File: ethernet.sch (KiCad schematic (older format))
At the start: 57 parts, among them J1701 RJ45, U1701 AR8031, Y1701 25MHz

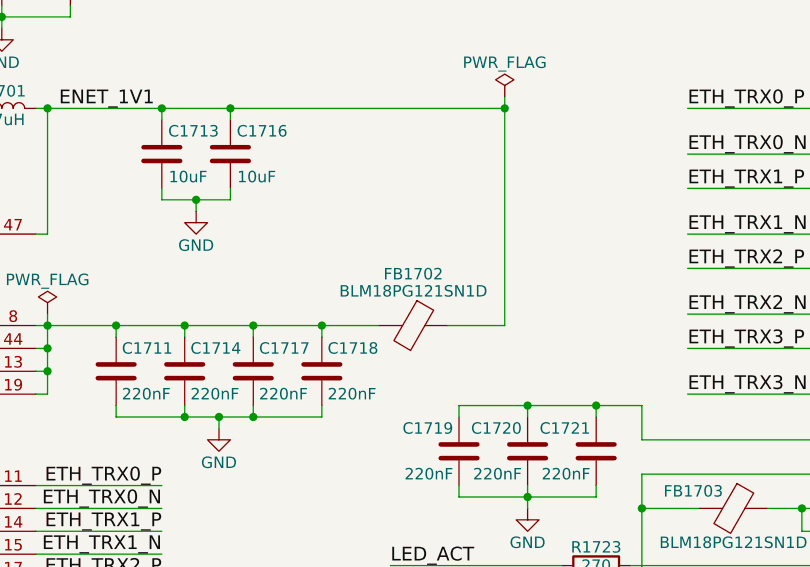
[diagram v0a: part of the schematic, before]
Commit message: Now using GPIO5_IO03 (P4.03) to put the class-D op-amp in shutdown and conserve energy when muted, make C1716 near the ETH PHY's DVDDL pin 47 220nF instead of 10uF (EmCraft suggested that this should be 100nF but their's is 220nF, asked why), added a 10k pull-down to PAM2841's ENA pin, added a 100nF cap to the smart card's C1 VCC pin, added a 1uF cap to the haptic motor circuit's 3V3_P rail
Still need to use I2C3 instead of I2C1 according to EmCraft's suggestions.
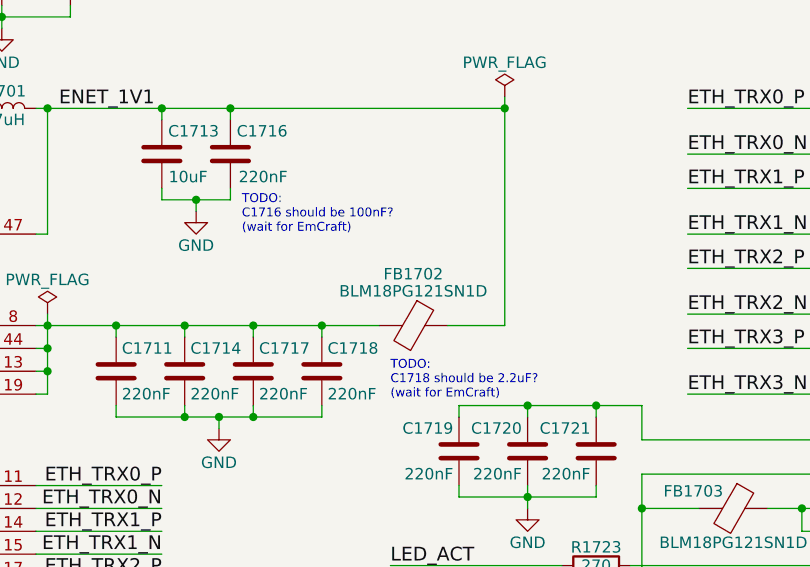
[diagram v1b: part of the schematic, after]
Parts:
- C1716: value 10uF -> 220nF
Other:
- note added: "TODO:\nC1716 should be 100nF?\n(wait for EmCraft)"
- note added: "TODO:\nC1718 should be 2.2uF?\n(wait for EmCraft)"
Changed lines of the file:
@@
 $EndComp
 $Comp
-L GND #PWR0296
+L GND #PWR0297
 U 1 1 5AF1A655
 P 5100 6650
-F 0 "#PWR0296" H 5100 6400 50  0001 C CNN
+F 0 "#PWR0297" H 5100 6400 50  0001 C CNN
 F 1 "GND" H 5100 6500 50  0000 C CNN
 F 2 "" H 5100 6650 50  0001 C CNN
@@
 $EndComp
 $Comp
-L GND #PWR0297
+L GND #PWR0298
 U 1 1 5AF1A6B7
 P 4000 6700
-F 0 "#PWR0297" H 4000 6450 50  0001 C CNN
+F 0 "#PWR0298" H 4000 6450 50  0001 C CNN
 F 1 "GND" H 4000 6550 50  0000 C CNN
 F 2 "" H 4000 6700 50  0001 C CNN
@@
 $EndComp
 $Comp
-L GND #PWR0298
+L GND #PWR0299
 U 1 1 5AF1C035
 P 3050 6900
-F 0 "#PWR0298" H 3050 6650 50  0001 C CNN
+F 0 "#PWR0299" H 3050 6650 50  0001 C CNN
 F 1 "GND" H 3050 6750 50  0000 C CNN
 F 2 "" H 3050 6900 50  0001 C CNN
@@
 $EndComp
 $Comp
-L GND #PWR0299
+L GND #PWR0300
 U 1 1 5AF1D077
 P 2150 6550
-F 0 "#PWR0299" H 2150 6300 50  0001 C CNN
+F 0 "#PWR0300" H 2150 6300 50  0001 C CNN
 F 1 "GND" H 2150 6400 50  0000 C CNN
 F 2 "" H 2150 6550 50  0001 C CNN
@@
 $EndComp
 $Comp
-L GND #PWR0300
+L GND #PWR0301
 U 1 1 5AF23D63
 P 6500 6550
-F 0 "#PWR0300" H 6500 6300 50  0001 C CNN
+F 0 "#PWR0301" H 6500 6300 50  0001 C CNN
 F 1 "GND" H 6500 6400 50  0000 C CNN
 F 2 "" H 6500 6550 50  0001 C CNN
@@
 $EndComp
 $Comp
-L GND #PWR0301
+L GND #PWR0302
 U 1 1 5AF27185
 P 6950 3550
-F 0 "#PWR0301" H 6950 3300 50  0001 C CNN
+F 0 "#PWR0302" H 6950 3300 50  0001 C CNN
 F 1 "GND" H 6950 3400 50  0000 C CNN
 F 2 "" H 6950 3550 50  0001 C CNN
@@
 $EndComp
 $Comp
-L GND #PWR0302
+L GND #PWR0303
 U 1 1 5AF2ADD1
 P 6850 2600
-F 0 "#PWR0302" H 6850 2350 50  0001 C CNN
+F 0 "#PWR0303" H 6850 2350 50  0001 C CNN
 F 1 "GND" H 6850 2450 50  0000 C CNN
 F 2 "" H 6850 2600 50  0001 C CNN
@@
 $EndComp
 $Comp
-L GND #PWR0303
+L GND #PWR0304
 U 1 1 5AF2DC02
 P 4200 1450
-F 0 "#PWR0303" H 4200 1200 50  0001 C CNN
+F 0 "#PWR0304" H 4200 1200 50  0001 C CNN
 F 1 "GND" H 4200 1300 50  0000 C CNN
 F 2 "" H 4200 1450 50  0001 C CNN
@@
 $EndComp
 $Comp
-L GND #PWR0304
+L GND #PWR0305
 U 1 1 5AF2E0B5
 P 4200 2100
-F 0 "#PWR0304" H 4200 1850 50  0001 C CNN
+F 0 "#PWR0305" H 4200 1850 50  0001 C CNN
 F 1 "GND" H 4200 1950 50  0000 C CNN
 F 2 "" H 4200 2100 50  0001 C CNN
@@
 $EndComp
 $Comp
-L 3V3_P #PWR0305
+L 3V3_P #PWR0306
 U 1 1 5AF325F5
 P 3000 950
-F 0 "#PWR0305" H 3000 800 50  0001 C CNN
+F 0 "#PWR0306" H 3000 800 50  0001 C CNN
 F 1 "3V3_P" H 3000 1090 50  0000 C CNN
 F 2 "" H 3000 950 50  0001 C CNN
@@
 $EndComp
 $Comp
-L GND #PWR0306
+L GND #PWR0307
 U 1 1 5AF33215
 P 6000 1800
-F 0 "#PWR0306" H 6000 1550 50  0001 C CNN
+F 0 "#PWR0307" H 6000 1550 50  0001 C CNN
 F 1 "GND" H 6000 1650 50  0000 C CNN
 F 2 "" H 6000 1800 50  0001 C CNN
@@
 ENET_2V5
 $Comp
-L 3V3_P #PWR0307
+L 3V3_P #PWR0308
 U 1 1 5AF58308
 P 2150 4500
-F 0 "#PWR0307" H 2150 4350 50  0001 C CNN
+F 0 "#PWR0308" H 2150 4350 50  0001 C CNN
 F 1 "3V3_P" H 2150 4640 50  0000 C CNN
 F 2 "" H 2150 4500 50  0001 C CNN
@@
 $EndComp
 $Comp
-L GND #PWR0308
+L GND #PWR0309
 U 1 1 5AFCAFF1
 P 1900 3550
-F 0 "#PWR0308" H 1900 3300 50  0001 C CNN
+F 0 "#PWR0309" H 1900 3300 50  0001 C CNN
 F 1 "GND" H 1900 3400 50  0000 C CNN
 F 2 "" H 1900 3550 50  0001 C CNN
@@
 $EndComp
 $Comp
-L GND #PWR0309
+L GND #PWR0310
 U 1 1 5B00F44D
 P 8800 5150
-F 0 "#PWR0309" H 8800 4900 50  0001 C CNN
+F 0 "#PWR0310" H 8800 4900 50  0001 C CNN
 F 1 "GND" H 8800 5000 50  0000 C CNN
 F 2 "" H 8800 5150 50  0001 C CNN
@@
 Connection ~ 7400 3100
 $Comp
-L GND #PWR0310
+L GND #PWR0311
 U 1 1 5B0467F8
 P 8300 3900
-F 0 "#PWR0310" H 8300 3650 50  0001 C CNN
+F 0 "#PWR0311" H 8300 3650 50  0001 C CNN
 F 1 "GND" H 8300 3750 50  0000 C CNN
 F 2 "" H 8300 3900 50  0001 C CNN
@@
 RGMII 10/100/1000 Ethernet
 $Comp
-L PWR_FLAG #FLG0311
+L PWR_FLAG #FLG0312
 U 1 1 5B0C2224
 P 4750 950
-F 0 "#FLG0311" H 4750 1025 50  0001 C CNN
+F 0 "#FLG0312" H 4750 1025 50  0001 C CNN
 F 1 "PWR_FLAG" H 4750 1100 50  0000 C CNN
 F 2 "" H 4750 950 50  0001 C CNN
@@
 Connection ~ 4750 1000
 $Comp
-L PWR_FLAG #FLG0312
+L PWR_FLAG #FLG0313
 U 1 1 5B0C422C
 P 8200 2100
-F 0 "#FLG0312" H 8200 2175 50  0001 C CNN
+F 0 "#FLG0313" H 8200 2175 50  0001 C CNN
 F 1 "PWR_FLAG" H 8200 2250 50  0000 C CNN
 F 2 "" H 8200 2100 50  0001 C CNN
@@
 Connection ~ 8200 2150
 $Comp
-L PWR_FLAG #FLG0313
+L PWR_FLAG #FLG0314
 U 1 1 5B0C4B7D
 P 6200 3050
-F 0 "#FLG0313" H 6200 3125 50  0001 C CNN
+F 0 "#FLG0314" H 6200 3125 50  0001 C CNN
 F 1 "PWR_FLAG" H 6200 3200 50  0000 C CNN
 F 2 "" H 6200 3050 50  0001 C CNN
@@
 P 7000 2350
 F 0 "C1716" H 6750 2450 50  0000 L CNN
-F 1 "10uF" H 6800 2250 50  0000 L CNN
+F 1 "220nF" H 6750 2250 50  0000 L CNN
 F 2 "Capacitors_SMD:C_0603" H 7038 2200 50  0001 C CNN
 F 3 "http://ds.yuden.co.jp/TYCOMPAS/ut/detail.do?productNo=LMK107BBJ106MALT&fileName=LMK107BBJ106MALT_SS&mode=specSheetDownload" H 7000 2350 50  0001 C CNN
@@
 Text Notes 3516 4832 0    39   ~ 0
 1%
+Text Notes 7700 3425 0    39   ~ 0
+TODO:\nC1718 should be 2.2uF?\n(wait for EmCraft)
+Text Notes 7050 2700 0    39   ~ 0
+TODO:\nC1716 should be 100nF?\n(wait for EmCraft)
 $EndSCHEMATC

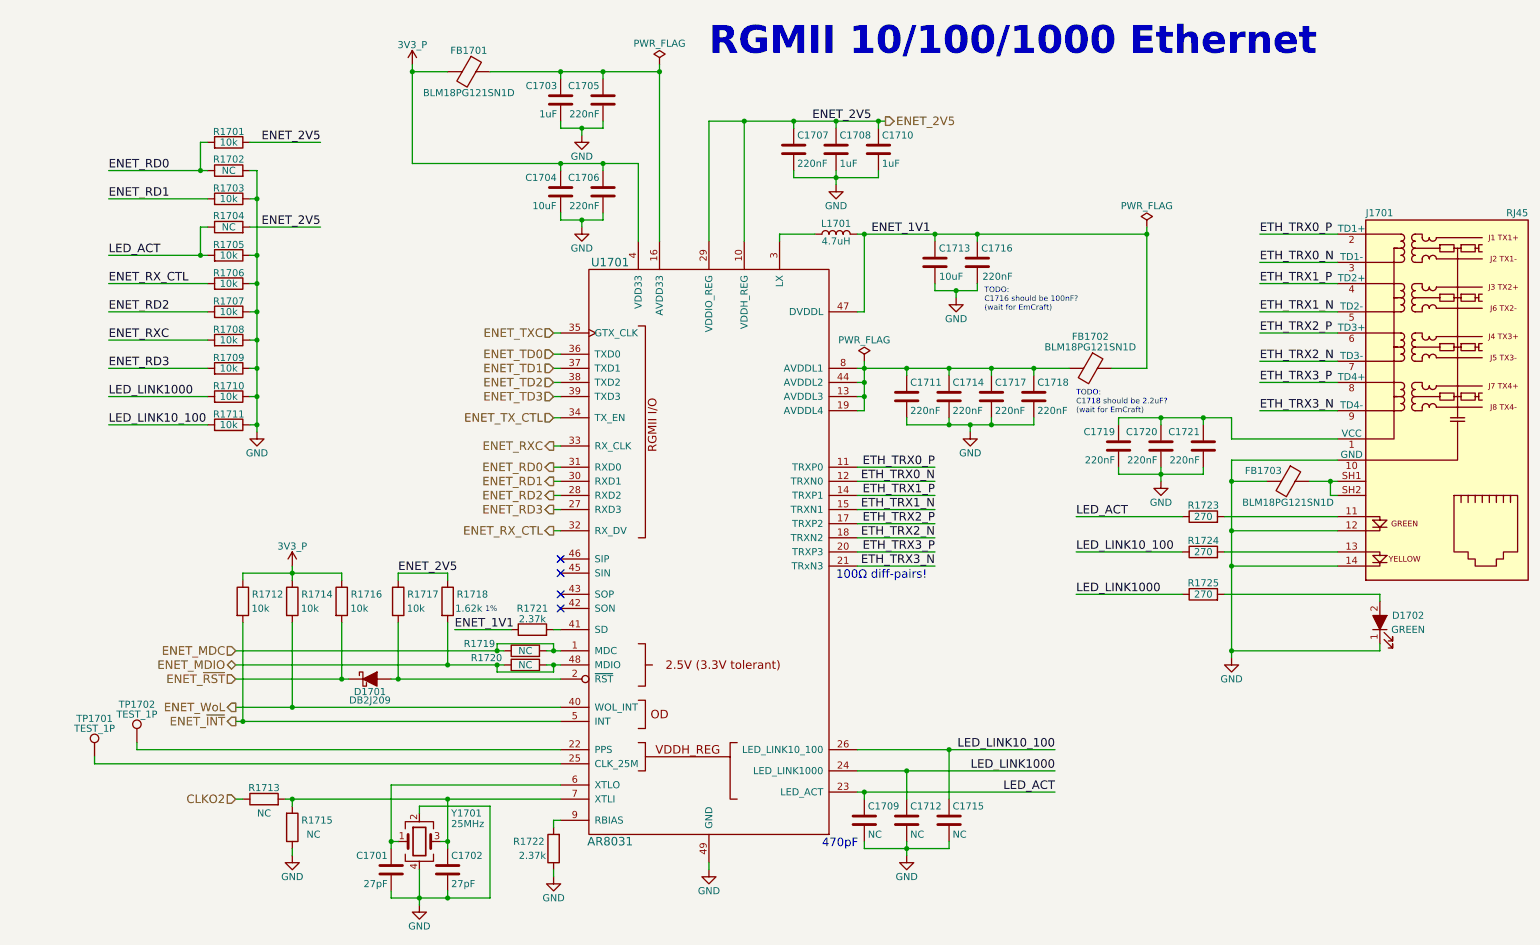
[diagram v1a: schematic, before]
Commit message: Change the capacitor C1718 near the ETH PHY's AVDDL2 pin 44 from 220nF to 2.2uF
Emcraft is also going to change this cap to 2.2uF.
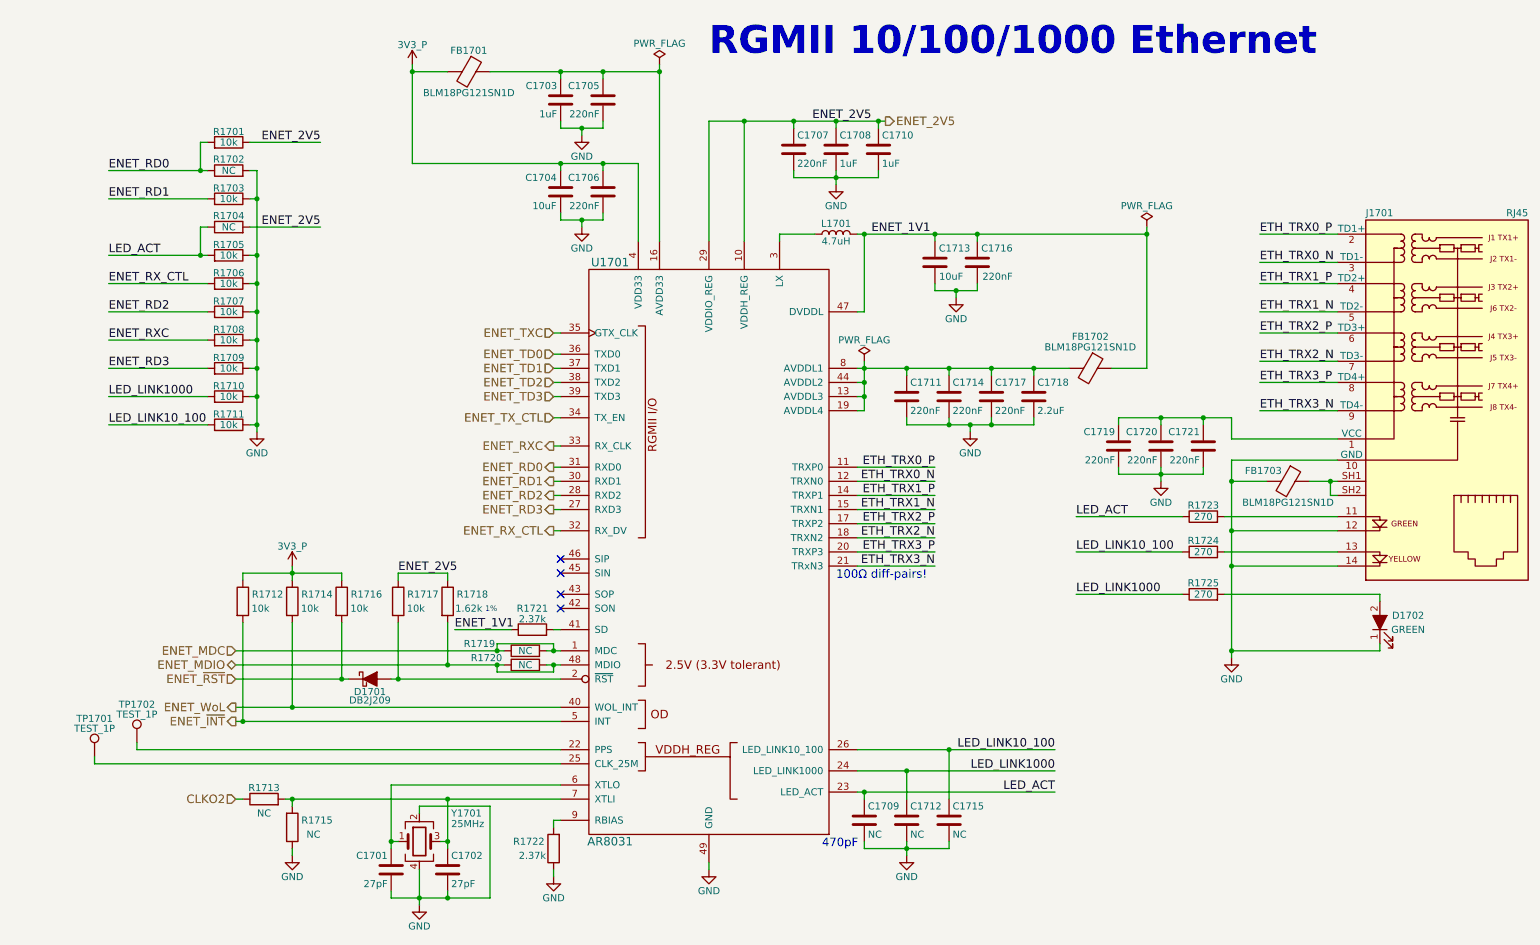
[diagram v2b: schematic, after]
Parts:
- C1718: value 220nF -> 2.2uF
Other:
- note removed: "TODO:\nC1716 should be 100nF?\n(wait for EmCraft)"
- note removed: "TODO:\nC1718 should be 2.2uF?\n(wait for EmCraft)"
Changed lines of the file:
@@
 	3050 6200 3550 6200
 Wire Wire Line
-	3550 6200 3550 6850
-Wire Wire Line
-	3550 6850 2850 6850
+	3550 6850 3550 6200
+Wire Wire Line
+	2850 6850 3550 6850
 Wire Wire Line
 	2850 6850 2850 6800
@@
 P 7400 3300
 F 0 "C1718" H 7425 3400 50  0000 L CNN
-F 1 "220nF" H 7425 3200 50  0000 L CNN
+F 1 "2.2uF" H 7425 3200 50  0000 L CNN
 F 2 "Capacitors_SMD:C_0603" H 7438 3150 50  0001 C CNN
 F 3 "" H 7400 3300 50  0001 C CNN
@@
 	9550 3600 8800 3600
 Wire Wire Line
-	8800 3600 8800 3450
+	8800 3450 8800 3600
 Wire Wire Line
 	8000 3450 8000 3500
@@
 $EndComp
 Wire Wire Line
-	8800 3450 8000 3450
+	8000 3450 8800 3450
 Wire Wire Line
 	8300 3800 8300 3900
@@
 Text Notes 3516 4832 0    39   ~ 0
 1%
-Text Notes 7700 3425 0    39   ~ 0
-TODO:\nC1718 should be 2.2uF?\n(wait for EmCraft)
-Text Notes 7050 2700 0    39   ~ 0
-TODO:\nC1716 should be 100nF?\n(wait for EmCraft)
 $EndSCHEMATC

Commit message: Move the charge controller, USB-C TCPC, and RTC to I2C1
Since each of these ICs will be powered at the same time as the SoM regardless of the PWR_EN state, they should share the same I2C bus as the PMIC.
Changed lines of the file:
@@
 $EndComp
 $Comp
-L GND #PWR0297
+L GND #PWR0298
 U 1 1 5AF1A655
 P 5100 6650
-F 0 "#PWR0297" H 5100 6400 50  0001 C CNN
+F 0 "#PWR0298" H 5100 6400 50  0001 C CNN
 F 1 "GND" H 5100 6500 50  0000 C CNN
 F 2 "" H 5100 6650 50  0001 C CNN
@@
 $EndComp
 $Comp
-L GND #PWR0298
+L GND #PWR0299
 U 1 1 5AF1A6B7
 P 4000 6700
-F 0 "#PWR0298" H 4000 6450 50  0001 C CNN
+F 0 "#PWR0299" H 4000 6450 50  0001 C CNN
 F 1 "GND" H 4000 6550 50  0000 C CNN
 F 2 "" H 4000 6700 50  0001 C CNN
@@
 $EndComp
 $Comp
-L GND #PWR0299
+L GND #PWR0300
 U 1 1 5AF1C035
 P 3050 6900
-F 0 "#PWR0299" H 3050 6650 50  0001 C CNN
+F 0 "#PWR0300" H 3050 6650 50  0001 C CNN
 F 1 "GND" H 3050 6750 50  0000 C CNN
 F 2 "" H 3050 6900 50  0001 C CNN
@@
 $EndComp
 $Comp
-L GND #PWR0300
+L GND #PWR0301
 U 1 1 5AF1D077
 P 2150 6550
-F 0 "#PWR0300" H 2150 6300 50  0001 C CNN
+F 0 "#PWR0301" H 2150 6300 50  0001 C CNN
 F 1 "GND" H 2150 6400 50  0000 C CNN
 F 2 "" H 2150 6550 50  0001 C CNN
@@
 $EndComp
 $Comp
-L GND #PWR0301
+L GND #PWR0302
 U 1 1 5AF23D63
 P 6500 6550
-F 0 "#PWR0301" H 6500 6300 50  0001 C CNN
+F 0 "#PWR0302" H 6500 6300 50  0001 C CNN
 F 1 "GND" H 6500 6400 50  0000 C CNN
 F 2 "" H 6500 6550 50  0001 C CNN
@@
 $EndComp
 $Comp
-L GND #PWR0302
+L GND #PWR0303
 U 1 1 5AF27185
 P 6950 3550
-F 0 "#PWR0302" H 6950 3300 50  0001 C CNN
+F 0 "#PWR0303" H 6950 3300 50  0001 C CNN
 F 1 "GND" H 6950 3400 50  0000 C CNN
 F 2 "" H 6950 3550 50  0001 C CNN
@@
 $EndComp
 $Comp
-L GND #PWR0303
+L GND #PWR0304
 U 1 1 5AF2ADD1
 P 6850 2600
-F 0 "#PWR0303" H 6850 2350 50  0001 C CNN
+F 0 "#PWR0304" H 6850 2350 50  0001 C CNN
 F 1 "GND" H 6850 2450 50  0000 C CNN
 F 2 "" H 6850 2600 50  0001 C CNN
@@
 $EndComp
 $Comp
-L GND #PWR0304
+L GND #PWR0305
 U 1 1 5AF2DC02
 P 4200 1450
-F 0 "#PWR0304" H 4200 1200 50  0001 C CNN
+F 0 "#PWR0305" H 4200 1200 50  0001 C CNN
 F 1 "GND" H 4200 1300 50  0000 C CNN
 F 2 "" H 4200 1450 50  0001 C CNN
@@
 $EndComp
 $Comp
-L GND #PWR0305
+L GND #PWR0306
 U 1 1 5AF2E0B5
 P 4200 2100
-F 0 "#PWR0305" H 4200 1850 50  0001 C CNN
+F 0 "#PWR0306" H 4200 1850 50  0001 C CNN
 F 1 "GND" H 4200 1950 50  0000 C CNN
 F 2 "" H 4200 2100 50  0001 C CNN
@@
 $EndComp
 $Comp
-L 3V3_P #PWR0306
+L 3V3_P #PWR0307
 U 1 1 5AF325F5
 P 3000 950
-F 0 "#PWR0306" H 3000 800 50  0001 C CNN
+F 0 "#PWR0307" H 3000 800 50  0001 C CNN
 F 1 "3V3_P" H 3000 1090 50  0000 C CNN
 F 2 "" H 3000 950 50  0001 C CNN
@@
 $EndComp
 $Comp
-L GND #PWR0307
+L GND #PWR0308
 U 1 1 5AF33215
 P 6000 1800
-F 0 "#PWR0307" H 6000 1550 50  0001 C CNN
+F 0 "#PWR0308" H 6000 1550 50  0001 C CNN
 F 1 "GND" H 6000 1650 50  0000 C CNN
 F 2 "" H 6000 1800 50  0001 C CNN
@@
 ENET_2V5
 $Comp
-L 3V3_P #PWR0308
+L 3V3_P #PWR0309
 U 1 1 5AF58308
 P 2150 4500
-F 0 "#PWR0308" H 2150 4350 50  0001 C CNN
+F 0 "#PWR0309" H 2150 4350 50  0001 C CNN
 F 1 "3V3_P" H 2150 4640 50  0000 C CNN
 F 2 "" H 2150 4500 50  0001 C CNN
@@
 $EndComp
 $Comp
-L GND #PWR0309
+L GND #PWR0310
 U 1 1 5AFCAFF1
 P 1900 3550
-F 0 "#PWR0309" H 1900 3300 50  0001 C CNN
+F 0 "#PWR0310" H 1900 3300 50  0001 C CNN
 F 1 "GND" H 1900 3400 50  0000 C CNN
 F 2 "" H 1900 3550 50  0001 C CNN
@@
 $EndComp
 $Comp
-L GND #PWR0310
+L GND #PWR0311
 U 1 1 5B00F44D
 P 8800 5150
-F 0 "#PWR0310" H 8800 4900 50  0001 C CNN
+F 0 "#PWR0311" H 8800 4900 50  0001 C CNN
 F 1 "GND" H 8800 5000 50  0000 C CNN
 F 2 "" H 8800 5150 50  0001 C CNN
@@
 	3050 6200 3550 6200
 Wire Wire Line
-	3550 6850 3550 6200
-Wire Wire Line
-	2850 6850 3550 6850
+	3550 6200 3550 6850
+Wire Wire Line
+	3550 6850 2850 6850
 Wire Wire Line
 	2850 6850 2850 6800
@@
 Connection ~ 7400 3100
 $Comp
-L GND #PWR0311
+L GND #PWR0312
 U 1 1 5B0467F8
 P 8300 3900
-F 0 "#PWR0311" H 8300 3650 50  0001 C CNN
+F 0 "#PWR0312" H 8300 3650 50  0001 C CNN
 F 1 "GND" H 8300 3750 50  0000 C CNN
 F 2 "" H 8300 3900 50  0001 C CNN
@@
 	9550 3600 8800 3600
 Wire Wire Line
-	8800 3450 8800 3600
+	8800 3600 8800 3450
 Wire Wire Line
 	8000 3450 8000 3500
@@
 RGMII 10/100/1000 Ethernet
 $Comp
-L PWR_FLAG #FLG0312
+L PWR_FLAG #FLG0313
 U 1 1 5B0C2224
 P 4750 950
-F 0 "#FLG0312" H 4750 1025 50  0001 C CNN
+F 0 "#FLG0313" H 4750 1025 50  0001 C CNN
 F 1 "PWR_FLAG" H 4750 1100 50  0000 C CNN
 F 2 "" H 4750 950 50  0001 C CNN
@@
 Connection ~ 4750 1000
 $Comp
-L PWR_FLAG #FLG0313
+L PWR_FLAG #FLG0314
 U 1 1 5B0C422C
 P 8200 2100
-F 0 "#FLG0313" H 8200 2175 50  0001 C CNN
+F 0 "#FLG0314" H 8200 2175 50  0001 C CNN
 F 1 "PWR_FLAG" H 8200 2250 50  0000 C CNN
 F 2 "" H 8200 2100 50  0001 C CNN
@@
 Connection ~ 8200 2150
 $Comp
-L PWR_FLAG #FLG0314
+L PWR_FLAG #FLG0315
 U 1 1 5B0C4B7D
 P 6200 3050
-F 0 "#FLG0314" H 6200 3125 50  0001 C CNN
+F 0 "#FLG0315" H 6200 3125 50  0001 C CNN
 F 1 "PWR_FLAG" H 6200 3200 50  0000 C CNN
 F 2 "" H 6200 3050 50  0001 C CNN
@@
 $EndComp
 Wire Wire Line
-	8000 3450 8800 3450
+	8800 3450 8000 3450
 Wire Wire Line
 	8300 3800 8300 3900
